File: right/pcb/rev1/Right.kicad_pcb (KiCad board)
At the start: 2 copper layers, 178.6 x 95.2 mm, 93 parts, among them SW1 SW_Push, U1 ATmega32U4-AU, U2 TRRS, Y1 16MHz

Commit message: Properly routed PCB
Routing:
- net +5V: track 182.6 -> 239.3 mm, vias 7 -> 9
- net GND: track 227.0 -> 279.2 mm, vias 2 -> 6

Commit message: Added more layouts to bottom spacebar
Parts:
- added MX39: MX-NoLED, MX_Only:MXOnly-2.75U-NoLED, F.Cu at (11.8, 178.6)
- added MX40: MX-NoLED, MX_Only:MXOnly-1U-NoLED, F.Cu at (47.5, 178.6)
- added MX9: MX-NoLED, MX_Only:MXOnly-1U-NoLED, F.Cu at (14.2, 159.5)
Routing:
- net col1: track 181.2 -> 201.8 mm
- net Net-(D5-Pad2): track 6.82 -> 21.4 mm
- net Net-(D10-Pad2): track 6.82 -> 20.8 mm, vias 0 -> 1
- net col0: track 208.8 -> 210.0 mm

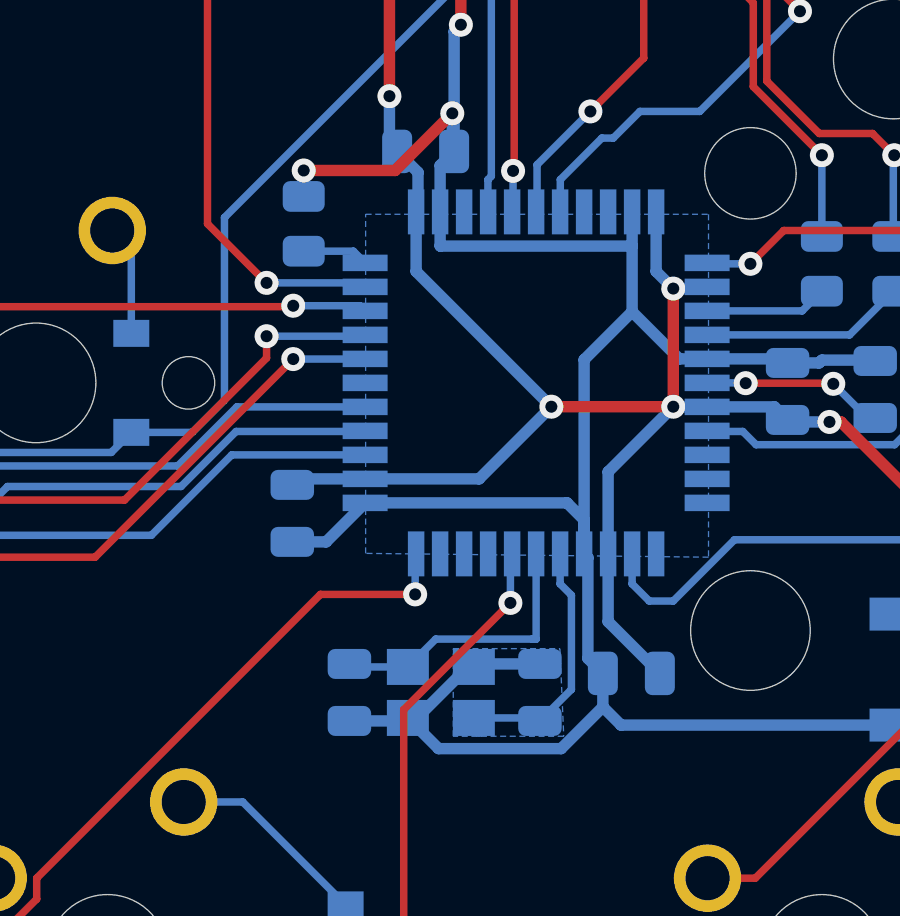
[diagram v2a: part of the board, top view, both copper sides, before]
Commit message: Fixed DRC issues
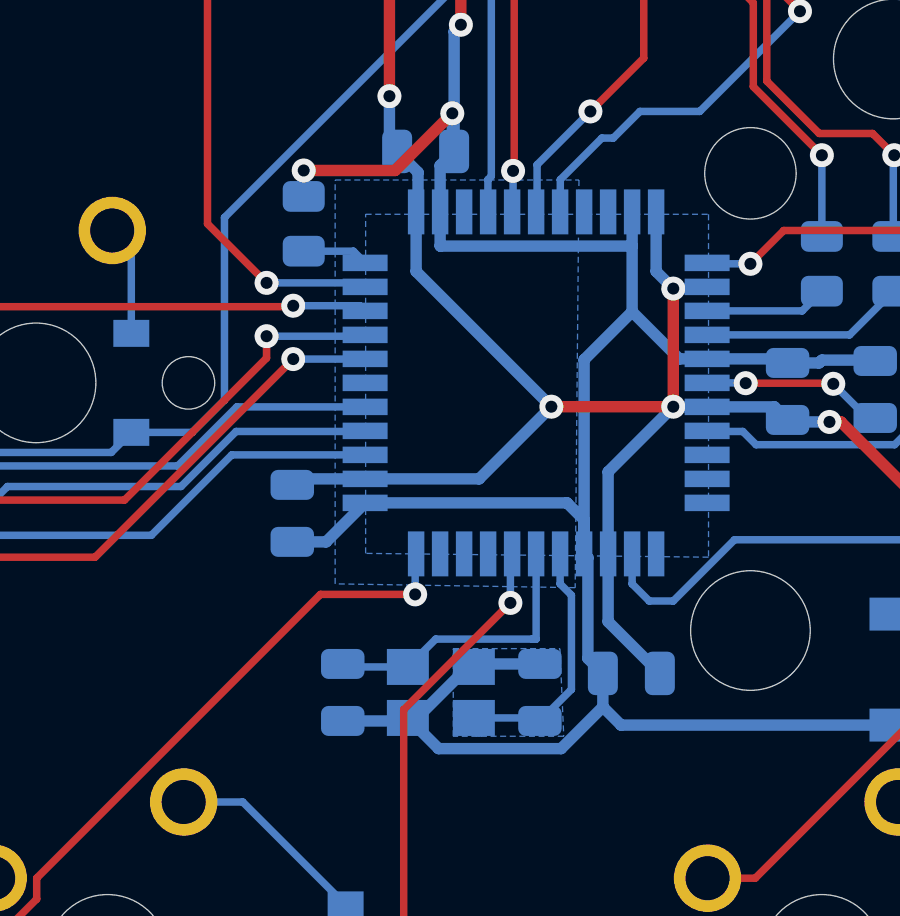
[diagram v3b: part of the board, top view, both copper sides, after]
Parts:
- moved C5 0.22 mm to (100.7, 169.9)
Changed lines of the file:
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@@
   )
   (module Capacitor_SMD:C_0805_2012Metric (layer B.Cu)
-    (at 100.93325 169.8625 270)
+    (at 100.711 169.8625 270)
     (descr "Capacitor SMD 0805 (2012 Metric), square (rectangular) end terminal, IPC_7351 nominal, (Body size source: IPC-SM-782 page 76, https://www.pcb-3d.com/wordpress/wp-content/uploads/ipc-sm-782a_amendment_1_and_2.pdf, https://docs.google.com/spreadsheets/d/1BsfQQcO9C6DZCsRaXUlFlo91Tg2WpOkGARC1WS5S8t0/edit?usp=sharing), generated with kicad-footprint-generator")
     (tags capacitor)
@@
       )
     )
+  )
+  (zone (net 1) (net_name GND) (layer B.Cu) (hatch edge 0.508)
+    (connect_pads (clearance 0.508))
+    (min_thickness 0.254)
+    (fill yes (arc_segments 32) (thermal_gap 0.508) (thermal_bridge_width 0.508))
+    (polygon
+      (pts
+        (xy 108.458 166.37) (xy 100.457 166.243) (xy 100.457 152.781) (xy 108.585 152.781)
+      )
+    )
